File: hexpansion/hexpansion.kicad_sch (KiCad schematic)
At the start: 17 parts, among them J1 Hexpansion-Connector, J2 Conn_01x08_Pin, U1 24LC00, U2 ATSHA204A-SSHDA

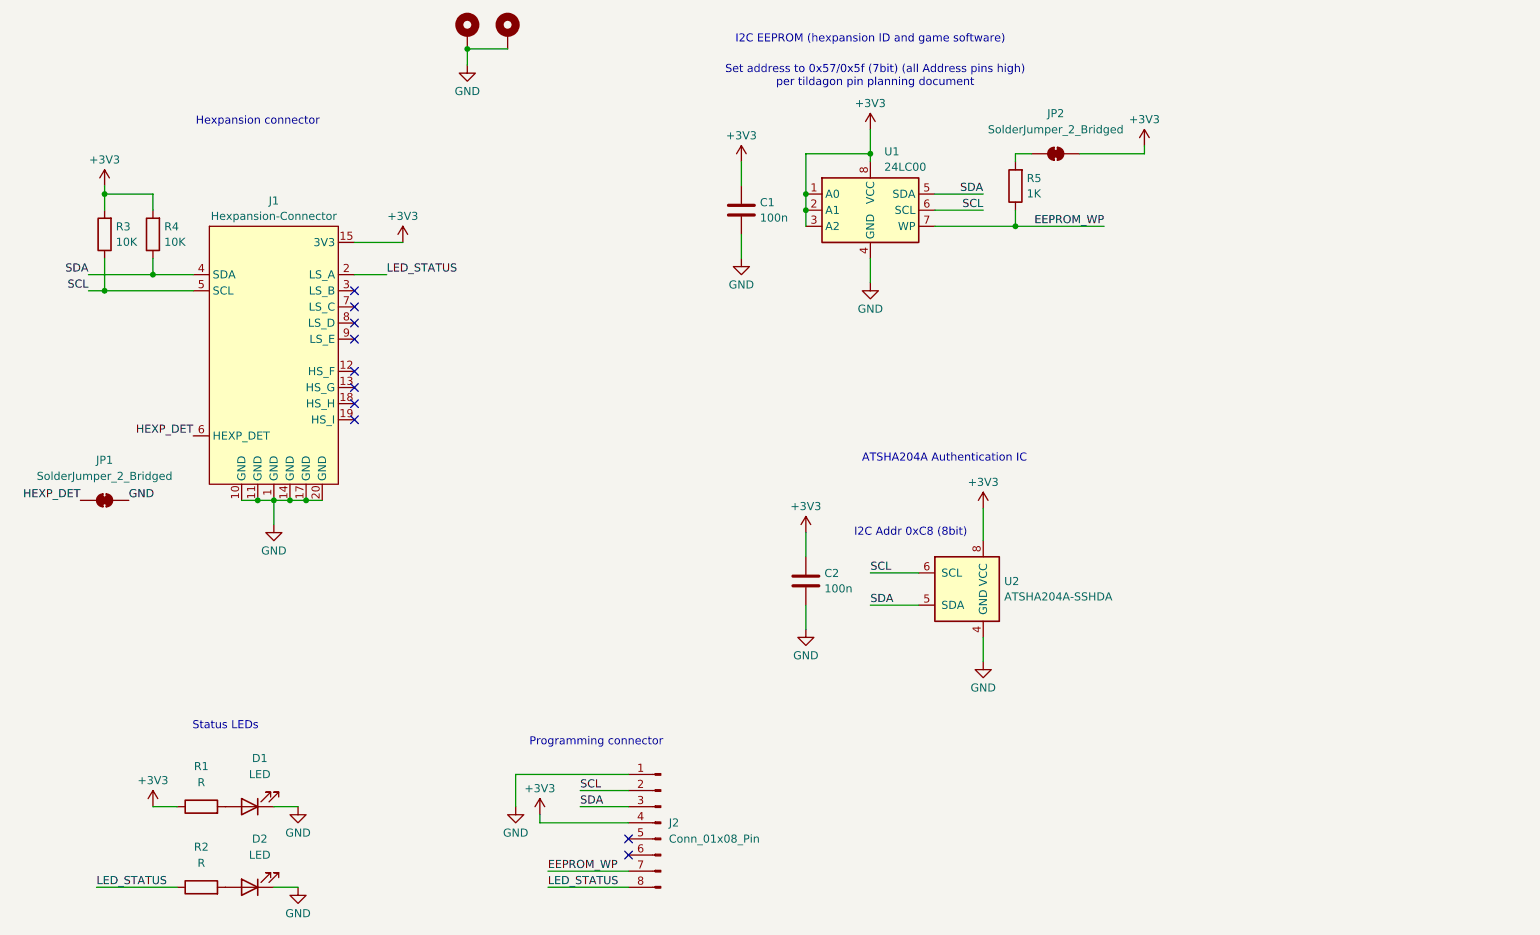
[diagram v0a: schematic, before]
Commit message: Update hexpansion design
Adds TVS diode
Removes seperate programming connector
tidy up PCB layout
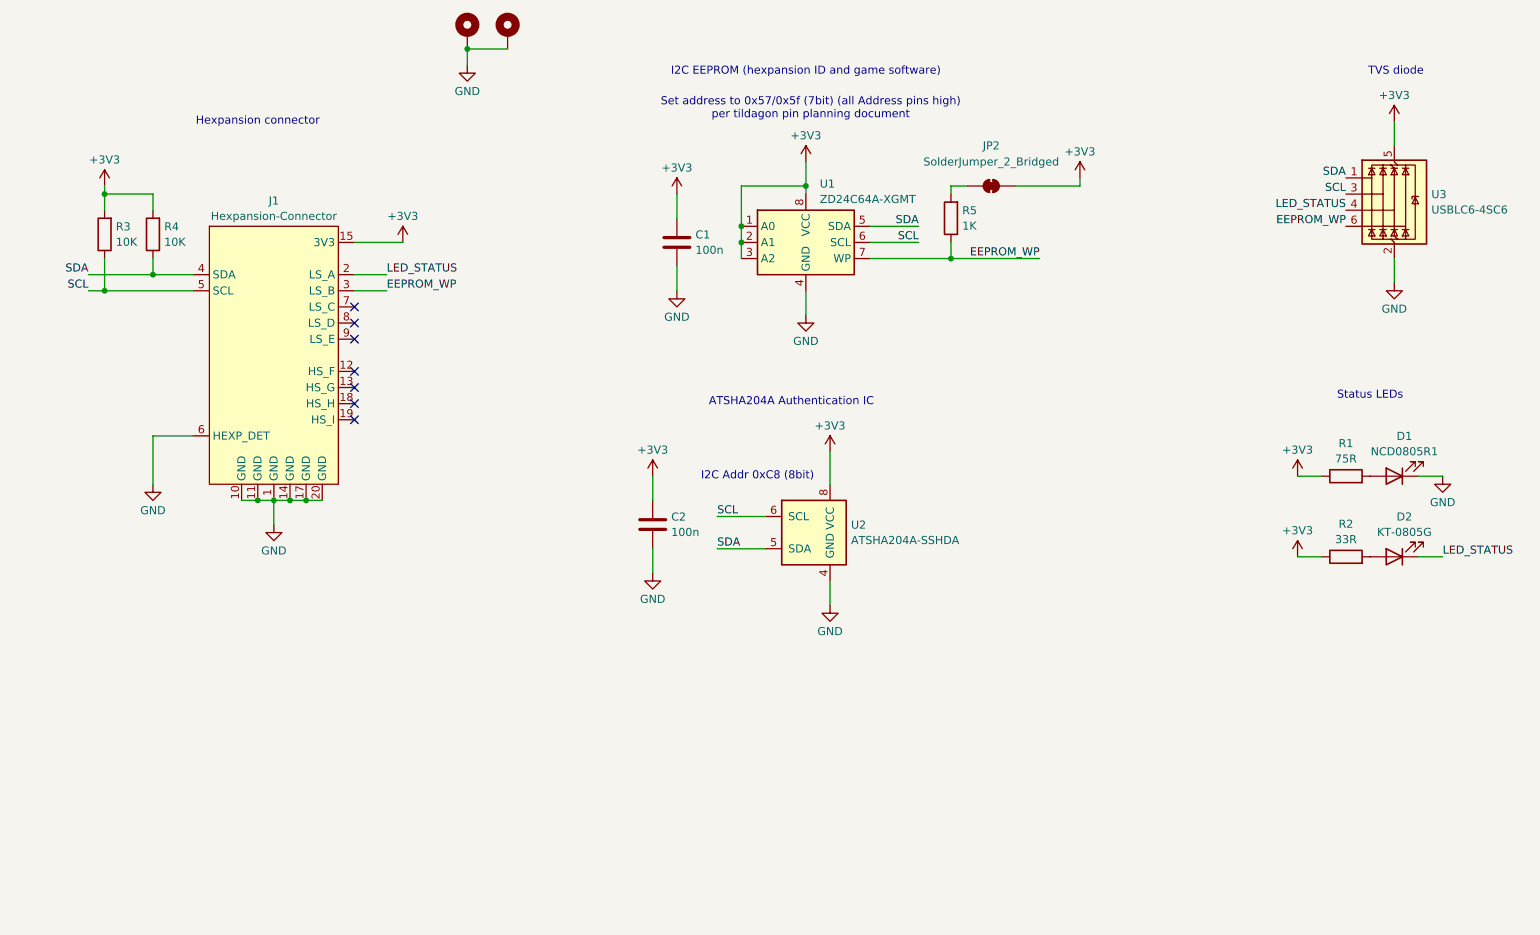
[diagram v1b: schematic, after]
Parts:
- removed J2: Conn_01x08_Pin, hexpansion:SOIC_clipProgSmall, symbol Connector:Conn_01x08_Pin
- removed JP1: SolderJumper_2_Bridged, Jumper:SolderJumper-2_P1.3mm_Bridged_RoundedPad1.0x1.5mm, symbol Jumper:SolderJumper_2_Bridged
- added U3: USBLC6-4SC6, Package_TO_SOT_SMD:SOT-23-6, symbol Power_Protection:WE-TVS-824015043
- D1: value LED -> NCD0805R1
- D2: value LED -> KT-0805G
- R1: value R -> 75R
- R2: value R -> 33R
- U1: value 24LC00 -> ZD24C64A-XGMT
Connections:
- net HEXP_DET is gone; now on net GND: J1.6 (HEXP_DET)
- net +3V3: now also R2.1, U3.5 (VBUS)
- net EEPROM_WP: now also J1.3 (LS_B), U3.6 (I/O4)
- net GND: now also U3.2 (GND); no longer D2.1 (K)
- net LED_STATUS: now also D2.1 (K), U3.4 (I/O3); no longer R2.1
- net SCL: now also U3.3 (I/O2)
- net SDA: now also U3.1 (I/O1)
- no-connect marks 10 -> 7
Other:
- note added: "TVS diode"
- note removed: "Programming connector"
- moved on the sheet: C1, C2, D1, D2, JP2, R1, R2, R5, U1, U2

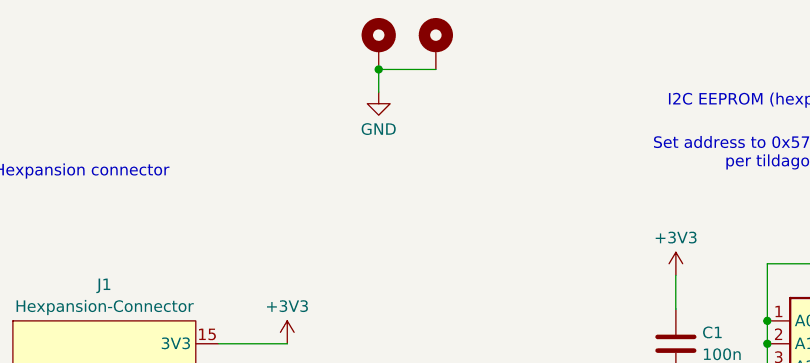
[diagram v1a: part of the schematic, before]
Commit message: Add pcb arwork and prep for manufacture.
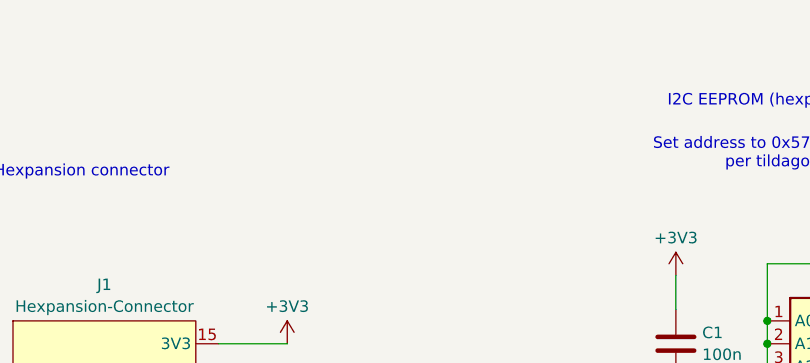
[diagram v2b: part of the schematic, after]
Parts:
- removed H1, H2: MountingHole_Pad, MountingHole:MountingHole_2.2mm_M2_Pad_Via, symbol Mechanical:MountingHole_Pad
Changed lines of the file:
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@@
-	)
-	(junction
-		(at 96.52 33.02)
-		(diameter 0)
-		(color 0 0 0 0)
 	)
 	(junction
@@
 	(wire
 		(pts
-			(xy 96.52 33.02) (xy 102.87 33.02)
-		)
-		(stroke
-			(width 0)
-			(type default)
-		)
-	)
-	(wire
-		(pts
 			(xy 63.5 104.14) (xy 66.04 104.14)
 		)
@@
 		(pts
 			(xy 53.34 93.98) (xy 46.99 93.98)
-		)
-		(stroke
-			(width 0)
-			(type default)
-		)
-	)
-	(wire
-		(pts
-			(xy 96.52 33.02) (xy 96.52 35.56)
 		)
 		(stroke
@@
 	)
 	(symbol
-		(lib_id "Mechanical:MountingHole_Pad")
-		(at 96.52 30.48 0)
-		(unit 1)
-		(exclude_from_sim no)
-		(in_bom yes)
-		(on_board yes)
-		(dnp no)
-		(fields_autoplaced yes)
-		(property "Reference" "H1"
-			(at 99.06 27.94 0)
-			(effects
-				(font
-					(size 1.27 1.27)
-				)
-				(justify left)
-				(hide yes)
-			)
-		)
-		(property "Value" "MountingHole_Pad"
-			(at 99.06 29.21 0)
-			(effects
-				(font
-					(size 1.27 1.27)
-				)
-				(justify left)
-				(hide yes)
-			)
-		)
-		(property "Footprint" "MountingHole:MountingHole_2.2mm_M2_Pad_Via"
-			(at 96.52 30.48 0)
-			(effects
-				(font
-					(size 1.27 1.27)
-				)
-				(hide yes)
-			)
-		)
-		(property "Datasheet" "~"
-			(at 96.52 30.48 0)
-			(effects
-				(font
-					(size 1.27 1.27)
-				)
-				(hide yes)
-			)
-		)
-		(property "Description" "Mounting Hole with connection"
-			(at 96.52 30.48 0)
-			(effects
-				(font
-					(size 1.27 1.27)
-				)
-				(hide yes)
-			)
-		)
-		(pin "1"
-		)
-		(instances
-			(project "hexpansion"
-				(path "/fb9bfa6e-c44d-469c-aa90-8ec28bcdf17f"
-					(reference "H1")
-					(unit 1)
-				)
-			)
-		)
-	)
-	(symbol
 		(lib_id "Device:LED")
 		(at 242.57 100.33 180)
@@
 	)
 	(symbol
-		(lib_id "power:GND")
-		(at 96.52 35.56 0)
-		(unit 1)
-		(exclude_from_sim no)
-		(in_bom yes)
-		(on_board yes)
-		(dnp no)
-		(fields_autoplaced yes)
-		(property "Reference" "#PWR03"
-			(at 96.52 41.91 0)
-			(effects
-				(font
-					(size 1.27 1.27)
-				)
-				(hide yes)
-			)
-		)
-		(property "Value" "GND"
-			(at 96.52 39.6931 0)
-			(effects
-				(font
-					(size 1.27 1.27)
-				)
-			)
-		)
-		(property "Footprint" ""
-			(at 96.52 35.56 0)
-			(effects
-				(font
-					(size 1.27 1.27)
-				)
-				(hide yes)
-			)
-		)
-		(property "Datasheet" ""
-			(at 96.52 35.56 0)
-			(effects
-				(font
-					(size 1.27 1.27)
-				)
-				(hide yes)
-			)
-		)
-		(property "Description" "Power symbol creates a global label with name \"GND\" , ground"
-			(at 96.52 35.56 0)
-			(effects
-				(font
-					(size 1.27 1.27)
-				)
-				(hide yes)
-			)
-		)
-		(pin "1"
-		)
-		(instances
-			(project "hexpansion"
-				(path "/fb9bfa6e-c44d-469c-aa90-8ec28bcdf17f"
-					(reference "#PWR03")
-					(unit 1)
-				)
-			)
-		)
-	)
-	(symbol
 		(lib_id "power:+3V3")
 		(at 149.86 50.8 0)
@@
 					(unit 1)
 				)
-			)
-		)
-	)
-	(symbol
-		(lib_id "Mechanical:MountingHole_Pad")
-		(at 102.87 30.48 0)
-		(unit 1)
-		(exclude_from_sim no)
-		(in_bom yes)
-		(on_board yes)
-		(dnp no)
-		(fields_autoplaced yes)
-		(property "Reference" "H2"
-			(at 105.41 27.94 0)
-			(effects
-				(font
-					(size 1.27 1.27)
-				)
-				(justify left)
-				(hide yes)
-			)
-		)
-		(property "Value" "MountingHole_Pad"
-			(at 105.41 29.21 0)
-			(effects
-				(font
-					(size 1.27 1.27)
-				)
-				(justify left)
-				(hide yes)
-			)
-		)
-		(property "Footprint" "MountingHole:MountingHole_2.2mm_M2_Pad_Via"
-			(at 102.87 30.48 0)
-			(effects
-				(font
-					(size 1.27 1.27)
-				)
-				(hide yes)
-			)
-		)
-		(property "Datasheet" "~"
-			(at 102.87 30.48 0)
-			(effects
-				(font
-					(size 1.27 1.27)
-				)
-				(hide yes)
-			)
-		)
-		(property "Description" "Mounting Hole with connection"
-			(at 102.87 30.48 0)
-			(effects
-				(font
-					(size 1.27 1.27)
-				)
-				(hide yes)
-			)
-		)
-		(pin "1"
-		)
-		(instances
-			(project "hexpansion"
-				(path "/fb9bfa6e-c44d-469c-aa90-8ec28bcdf17f"
-					(reference "H2")
-					(unit 1)
-				)
